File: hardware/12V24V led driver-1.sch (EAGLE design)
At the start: 30 parts, among them X1 USB-MICROB

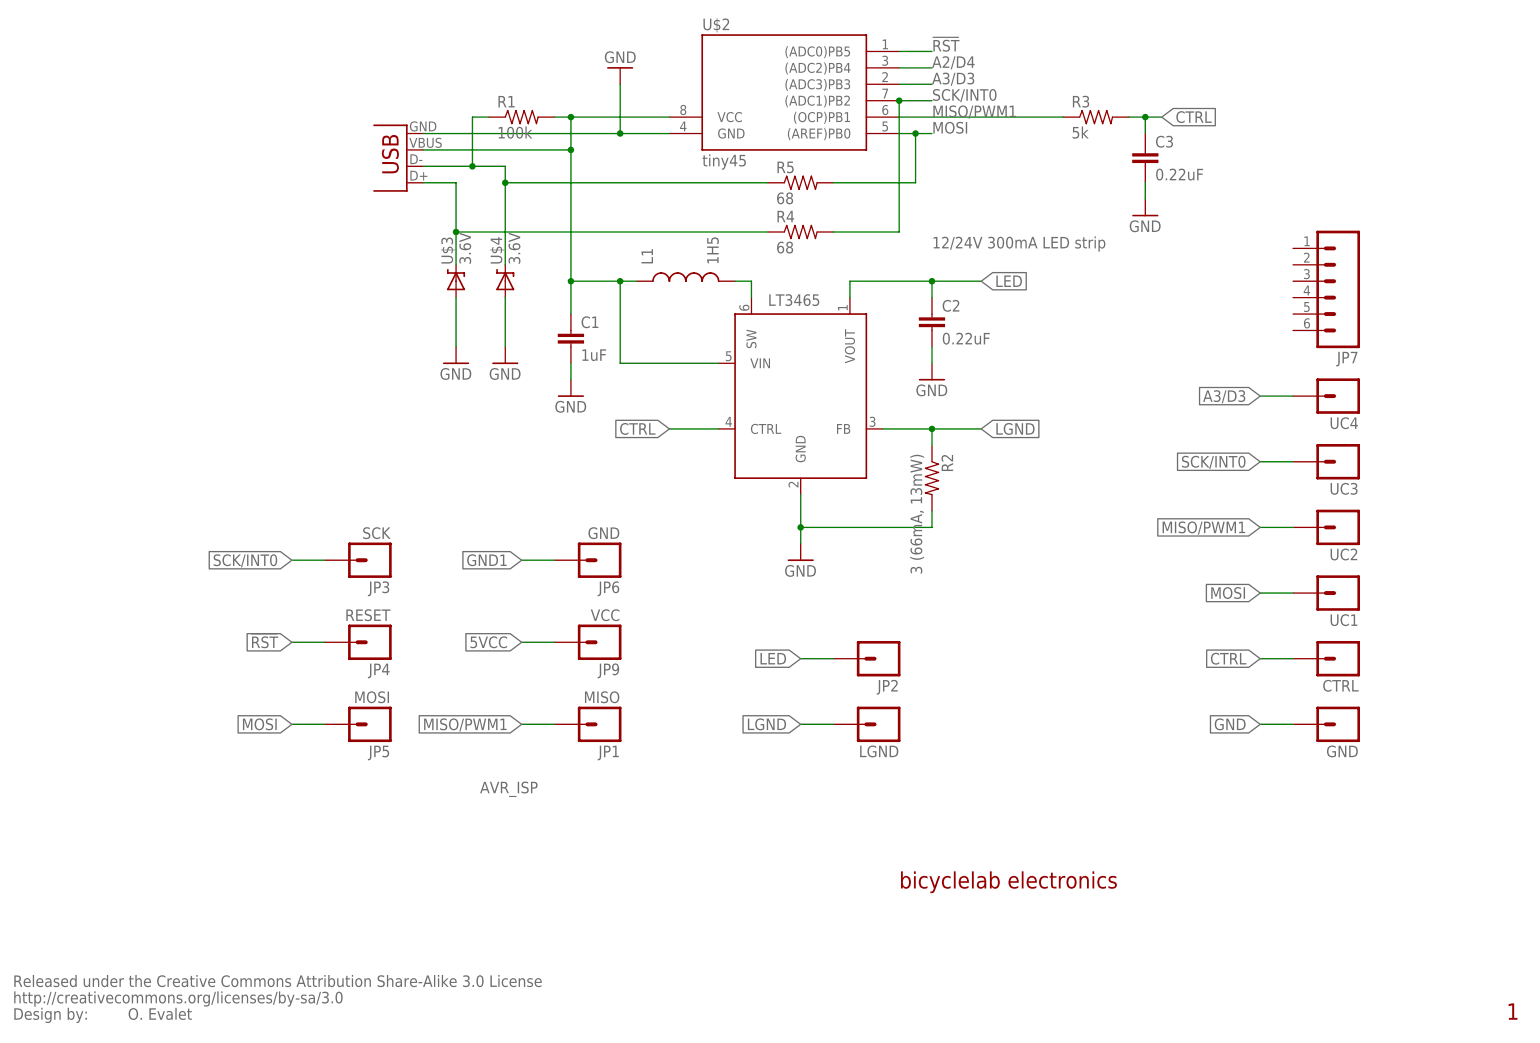
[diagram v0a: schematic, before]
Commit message: usb ctrl imp.
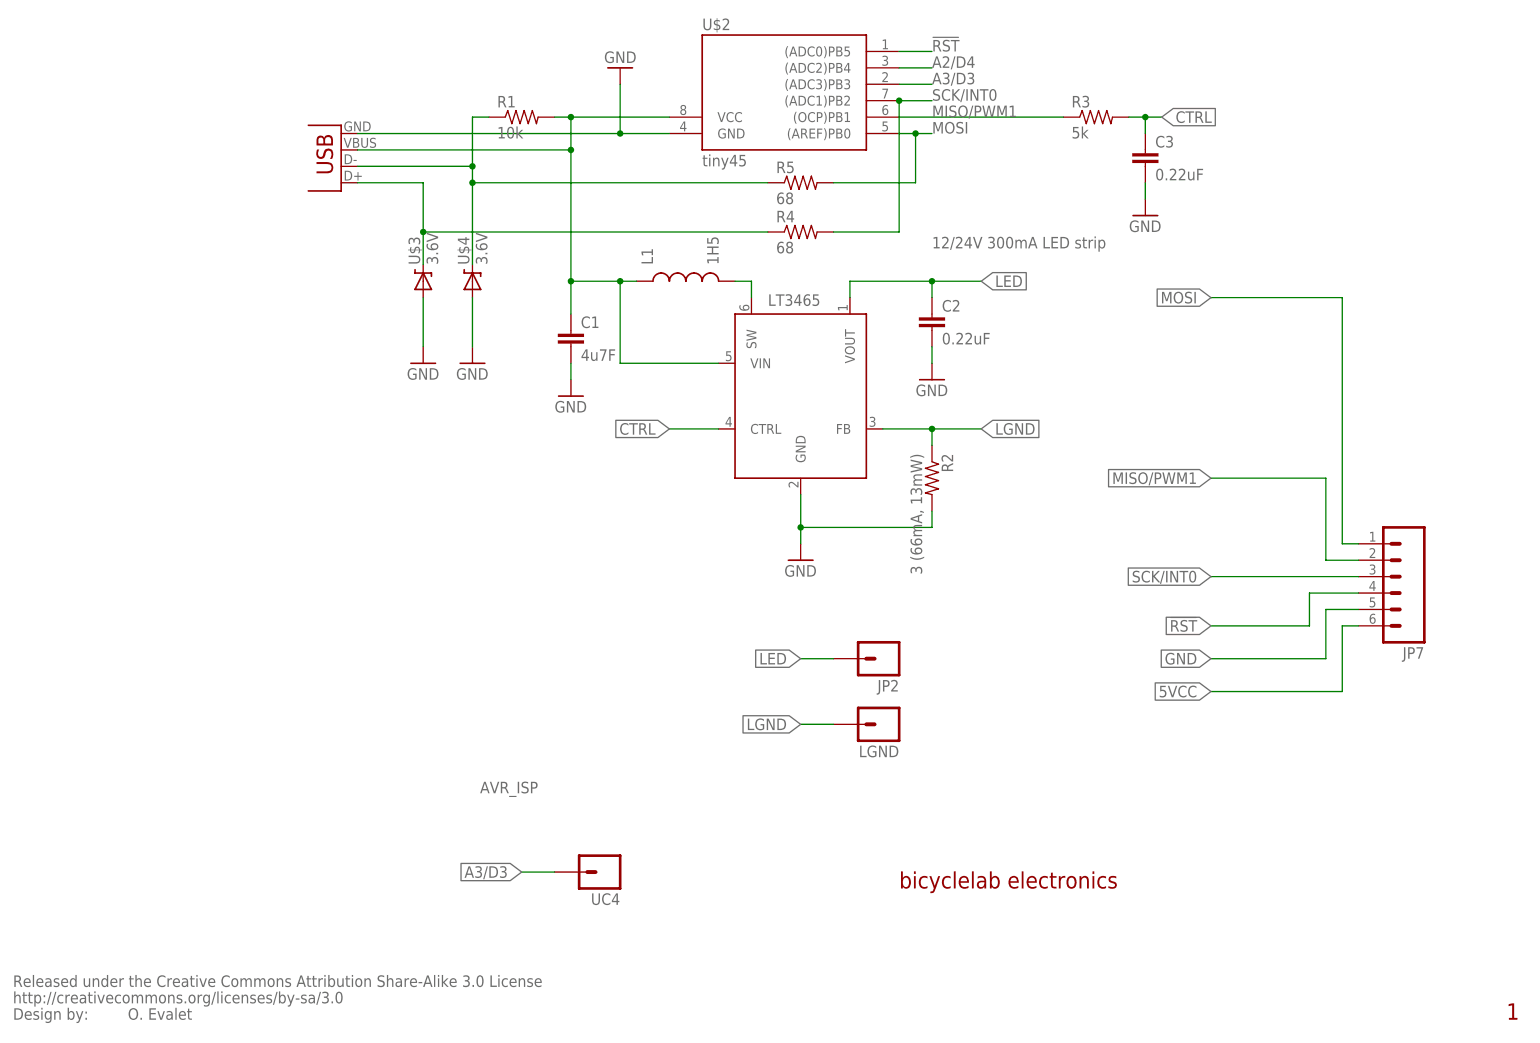
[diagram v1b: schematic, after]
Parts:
- removed CTRL, GND, UC1, UC2, UC3: M01SMDNS, SparkFun:M01SMDNS
- removed JP1: MISO, bicyclelab:M01SMD-TINY
- removed JP3: SCK, bicyclelab:M01SMD-TINY
- removed JP4: RESET, bicyclelab:M01SMD-TINY
- removed JP5: MOSI, bicyclelab:M01SMD-TINY
- removed JP6: GND, bicyclelab:M01SMD-TINY
- removed JP9: VCC, bicyclelab:M01SMD-TINY
- removed X1: USB-MICROB, 0-SparkFun:USB-MICROB
- added MISB-SW-5B: MISB-SW-5B, 0-SparkFun:USB-MICROB
- C1: value 1uF -> 4u7F
- R1: value 100k -> 10k
- UC4: value M01SMDNS -> M01SMD-4.5X1.5; device SparkFun:M01SMDNS -> SparkFun:M01SMD-4.5X1.5
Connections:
- removed net GND1: JP6.1
- net !RST: now also JP7.4; no longer JP4.1
- net 5VCC: now also JP7.6, MISB-SW-5B.VBUS; no longer JP9.1, X1.VBUS
- net CTRL: no longer CTRL.1
- net GND: now also JP7.5, MISB-SW-5B.GND; no longer GND.1, X1.GND
- net MISO/PWM1: now also JP7.2; no longer JP1.1, UC2.1
- net MOSI: now also JP7.1; no longer JP5.1, UC1.1
- net N$1: now also MISB-SW-5B.D+; no longer X1.D+
- net N$2: now also MISB-SW-5B.D-; no longer X1.D-
- net SCK/INT0: now also JP7.3; no longer JP3.1, UC3.1
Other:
- moved on the sheet: JP7, U$3, U$4, UC4

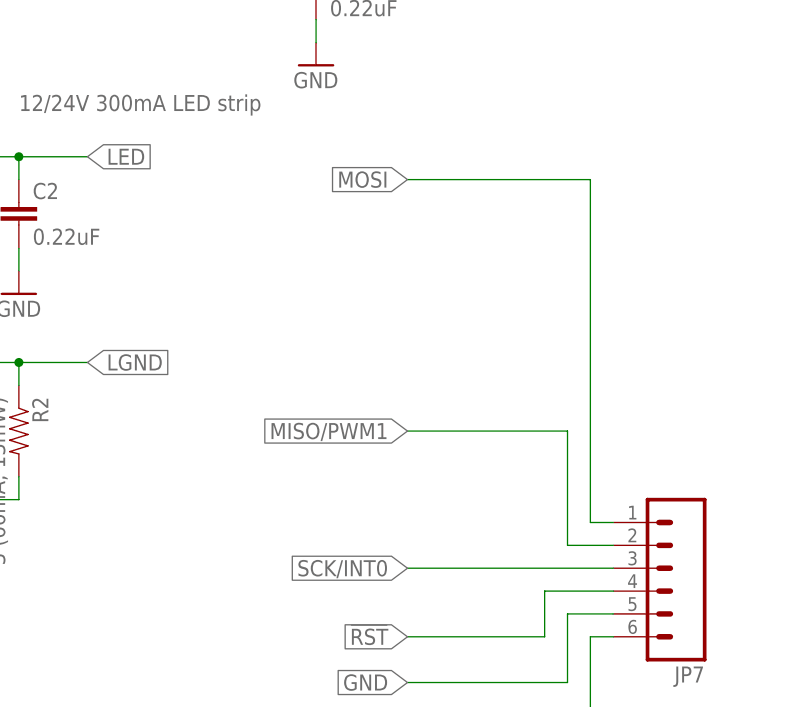
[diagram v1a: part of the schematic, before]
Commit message: usb ctrl imp.
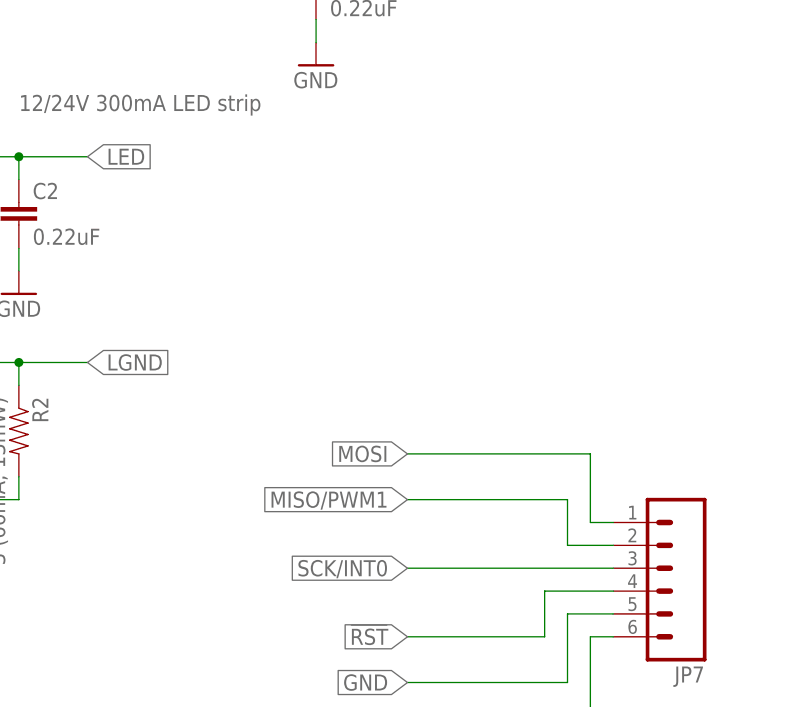
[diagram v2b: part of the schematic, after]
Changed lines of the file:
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@@
 <grid distance="0.1" unitdist="inch" unit="inch" style="lines" multiple="1" display="no" altdistance="0.01" altunitdist="inch" altunit="inch"/>
 <layers>
-<layer number="1" name="Top" color="4" fill="1" visible="yes" active="no"/>
-<layer number="2" name="Route2" color="1" fill="3" visible="yes" active="no"/>
-<layer number="3" name="Route3" color="4" fill="3" visible="yes" active="no"/>
-<layer number="4" name="Route4" color="1" fill="4" visible="yes" active="no"/>
-<layer number="5" name="Route5" color="4" fill="4" visible="yes" active="no"/>
-<layer number="6" name="Route6" color="1" fill="8" visible="yes" active="no"/>
-<layer number="7" name="Route7" color="4" fill="8" visible="yes" active="no"/>
-<layer number="8" name="Route8" color="1" fill="2" visible="yes" active="no"/>
-<layer number="9" name="Route9" color="4" fill="2" visible="yes" active="no"/>
-<layer number="10" name="Route10" color="1" fill="7" visible="yes" active="no"/>
-<layer number="11" name="Route11" color="4" fill="7" visible="yes" active="no"/>
-<layer number="12" name="Route12" color="1" fill="5" visible="yes" active="no"/>
-<layer number="13" name="Route13" color="4" fill="5" visible="yes" active="no"/>
-<layer number="14" name="Route14" color="1" fill="6" visible="yes" active="no"/>
-<layer number="15" name="Route15" color="4" fill="6" visible="yes" active="no"/>
-<layer number="16" name="Bottom" color="1" fill="1" visible="yes" active="no"/>
-<layer number="17" name="Pads" color="2" fill="1" visible="yes" active="no"/>
-<layer number="18" name="Vias" color="2" fill="1" visible="yes" active="no"/>
-<layer number="19" name="Unrouted" color="6" fill="1" visible="yes" active="no"/>
-<layer number="20" name="Dimension" color="15" fill="1" visible="yes" active="no"/>
-<layer number="21" name="tPlace" color="14" fill="1" visible="yes" active="no"/>
-<layer number="22" name="bPlace" color="14" fill="1" visible="yes" active="no"/>
-<layer number="23" name="tOrigins" color="15" fill="1" visible="yes" active="no"/>
-<layer number="24" name="bOrigins" color="15" fill="1" visible="yes" active="no"/>
-<layer number="25" name="tNames" color="7" fill="1" visible="yes" active="no"/>
-<layer number="26" name="bNames" color="7" fill="1" visible="yes" active="no"/>
-<layer number="27" name="tValues" color="7" fill="1" visible="yes" active="no"/>
-<layer number="28" name="bValues" color="7" fill="1" visible="yes" active="no"/>
+<layer number="1" name="Top" color="4" fill="1" visible="no" active="no"/>
+<layer number="2" name="Route2" color="1" fill="3" visible="no" active="no"/>
+<layer number="3" name="Route3" color="4" fill="3" visible="no" active="no"/>
+<layer number="4" name="Route4" color="1" fill="4" visible="no" active="no"/>
+<layer number="5" name="Route5" color="4" fill="4" visible="no" active="no"/>
+<layer number="6" name="Route6" color="1" fill="8" visible="no" active="no"/>
+<layer number="7" name="Route7" color="4" fill="8" visible="no" active="no"/>
+<layer number="8" name="Route8" color="1" fill="2" visible="no" active="no"/>
+<layer number="9" name="Route9" color="4" fill="2" visible="no" active="no"/>
+<layer number="10" name="Route10" color="1" fill="7" visible="no" active="no"/>
+<layer number="11" name="Route11" color="4" fill="7" visible="no" active="no"/>
+<layer number="12" name="Route12" color="1" fill="5" visible="no" active="no"/>
+<layer number="13" name="Route13" color="4" fill="5" visible="no" active="no"/>
+<layer number="14" name="Route14" color="1" fill="6" visible="no" active="no"/>
+<layer number="15" name="Route15" color="4" fill="6" visible="no" active="no"/>
+<layer number="16" name="Bottom" color="1" fill="1" visible="no" active="no"/>
+<layer number="17" name="Pads" color="2" fill="1" visible="no" active="no"/>
+<layer number="18" name="Vias" color="2" fill="1" visible="no" active="no"/>
+<layer number="19" name="Unrouted" color="6" fill="1" visible="no" active="no"/>
+<layer number="20" name="Dimension" color="15" fill="1" visible="no" active="no"/>
+<layer number="21" name="tPlace" color="14" fill="1" visible="no" active="no"/>
+<layer number="22" name="bPlace" color="14" fill="1" visible="no" active="no"/>
+<layer number="23" name="tOrigins" color="15" fill="1" visible="no" active="no"/>
+<layer number="24" name="bOrigins" color="15" fill="1" visible="no" active="no"/>
+<layer number="25" name="tNames" color="7" fill="1" visible="no" active="no"/>
+<layer number="26" name="bNames" color="7" fill="1" visible="no" active="no"/>
+<layer number="27" name="tValues" color="7" fill="1" visible="no" active="no"/>
+<layer number="28" name="bValues" color="7" fill="1" visible="no" active="no"/>
 <layer number="29" name="tStop" color="7" fill="3" visible="no" active="no"/>
 <layer number="30" name="bStop" color="7" fill="6" visible="no" active="no"/>
@@
 <layer number="35" name="tGlue" color="7" fill="4" visible="no" active="no"/>
 <layer number="36" name="bGlue" color="7" fill="5" visible="no" active="no"/>
-<layer number="37" name="tTest" color="7" fill="1" visible="yes" active="no"/>
-<layer number="38" name="bTest" color="7" fill="1" visible="yes" active="no"/>
+<layer number="37" name="tTest" color="7" fill="1" visible="no" active="no"/>
+<layer number="38" name="bTest" color="7" fill="1" visible="no" active="no"/>
 <layer number="39" name="tKeepout" color="4" fill="11" visible="no" active="no"/>
 <layer number="40" name="bKeepout" color="1" fill="11" visible="no" active="no"/>
@@
 <layer number="44" name="Drills" color="7" fill="1" visible="no" active="no"/>
 <layer number="45" name="Holes" color="7" fill="1" visible="no" active="no"/>
-<layer number="46" name="Milling" color="3" fill="1" visible="yes" active="no"/>
-<layer number="47" name="Measures" color="7" fill="1" visible="yes" active="no"/>
-<layer number="48" name="Document" color="7" fill="1" visible="yes" active="no"/>
-<layer number="49" name="Reference" color="7" fill="1" visible="yes" active="no"/>
-<layer number="50" name="dxf" color="7" fill="1" visible="yes" active="no"/>
-<layer number="51" name="tDocu" color="7" fill="1" visible="yes" active="no"/>
-<layer number="52" name="bDocu" color="7" fill="1" visible="yes" active="no"/>
-<layer number="53" name="tGND_GNDA" color="7" fill="9" visible="yes" active="no"/>
-<layer number="54" name="bGND_GNDA" color="1" fill="9" visible="yes" active="no"/>
-<layer number="56" name="wert" color="7" fill="1" visible="yes" active="no"/>
+<layer number="46" name="Milling" color="3" fill="1" visible="no" active="no"/>
+<layer number="47" name="Measures" color="7" fill="1" visible="no" active="no"/>
+<layer number="48" name="Document" color="7" fill="1" visible="no" active="no"/>
+<layer number="49" name="Reference" color="7" fill="1" visible="no" active="no"/>
+<layer number="50" name="dxf" color="7" fill="1" visible="no" active="no"/>
+<layer number="51" name="tDocu" color="7" fill="1" visible="no" active="no"/>
+<layer number="52" name="bDocu" color="7" fill="1" visible="no" active="no"/>
+<layer number="53" name="tGND_GNDA" color="7" fill="9" visible="no" active="no"/>
+<layer number="54" name="bGND_GNDA" color="1" fill="9" visible="no" active="no"/>
+<layer number="56" name="wert" color="7" fill="1" visible="no" active="no"/>
 <layer number="91" name="Nets" color="2" fill="1" visible="yes" active="yes"/>
 <layer number="92" name="Busses" color="1" fill="1" visible="yes" active="yes"/>
@@
 </segment>
 <segment>
-<label x="198.12" y="119.38" size="1.778" layer="95" rot="R180" xref="yes"/>
+<label x="198.12" y="88.9" size="1.778" layer="95" rot="R180" xref="yes"/>
 <pinref part="JP7" gate="G$1" pin="1"/>
 <wire x1="220.98" y1="81.28" x2="218.44" y2="81.28" width="0.1524" layer="91"/>
-<wire x1="218.44" y1="81.28" x2="218.44" y2="119.38" width="0.1524" layer="91"/>
-<wire x1="218.44" y1="119.38" x2="198.12" y2="119.38" width="0.1524" layer="91"/>
+<wire x1="218.44" y1="81.28" x2="218.44" y2="88.9" width="0.1524" layer="91"/>
+<wire x1="218.44" y1="88.9" x2="198.12" y2="88.9" width="0.1524" layer="91"/>
 </segment>
 </net>
@@
 </segment>
 <segment>
-<label x="198.12" y="91.44" size="1.778" layer="95" rot="R180" xref="yes"/>
+<label x="198.12" y="83.82" size="1.778" layer="95" rot="R180" xref="yes"/>
 <pinref part="JP7" gate="G$1" pin="2"/>
 <wire x1="220.98" y1="78.74" x2="215.9" y2="78.74" width="0.1524" layer="91"/>
-<wire x1="215.9" y1="78.74" x2="215.9" y2="91.44" width="0.1524" layer="91"/>
-<wire x1="215.9" y1="91.44" x2="198.12" y2="91.44" width="0.1524" layer="91"/>
-</segment>
-</net>
+<wire x1="215.9" y1="78.74" x2="215.9" y2="83.82" width="0.1524" layer="91"/>
+<wire x1="215.9" y1="83.82" x2="198.12" y2="83.82" width="0.1524" layer="91"/>
+</segment>
+</net>
